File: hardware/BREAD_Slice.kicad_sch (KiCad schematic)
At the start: 15 parts, among them J1 Conn_01x10_Female, J2 I2C_01x04

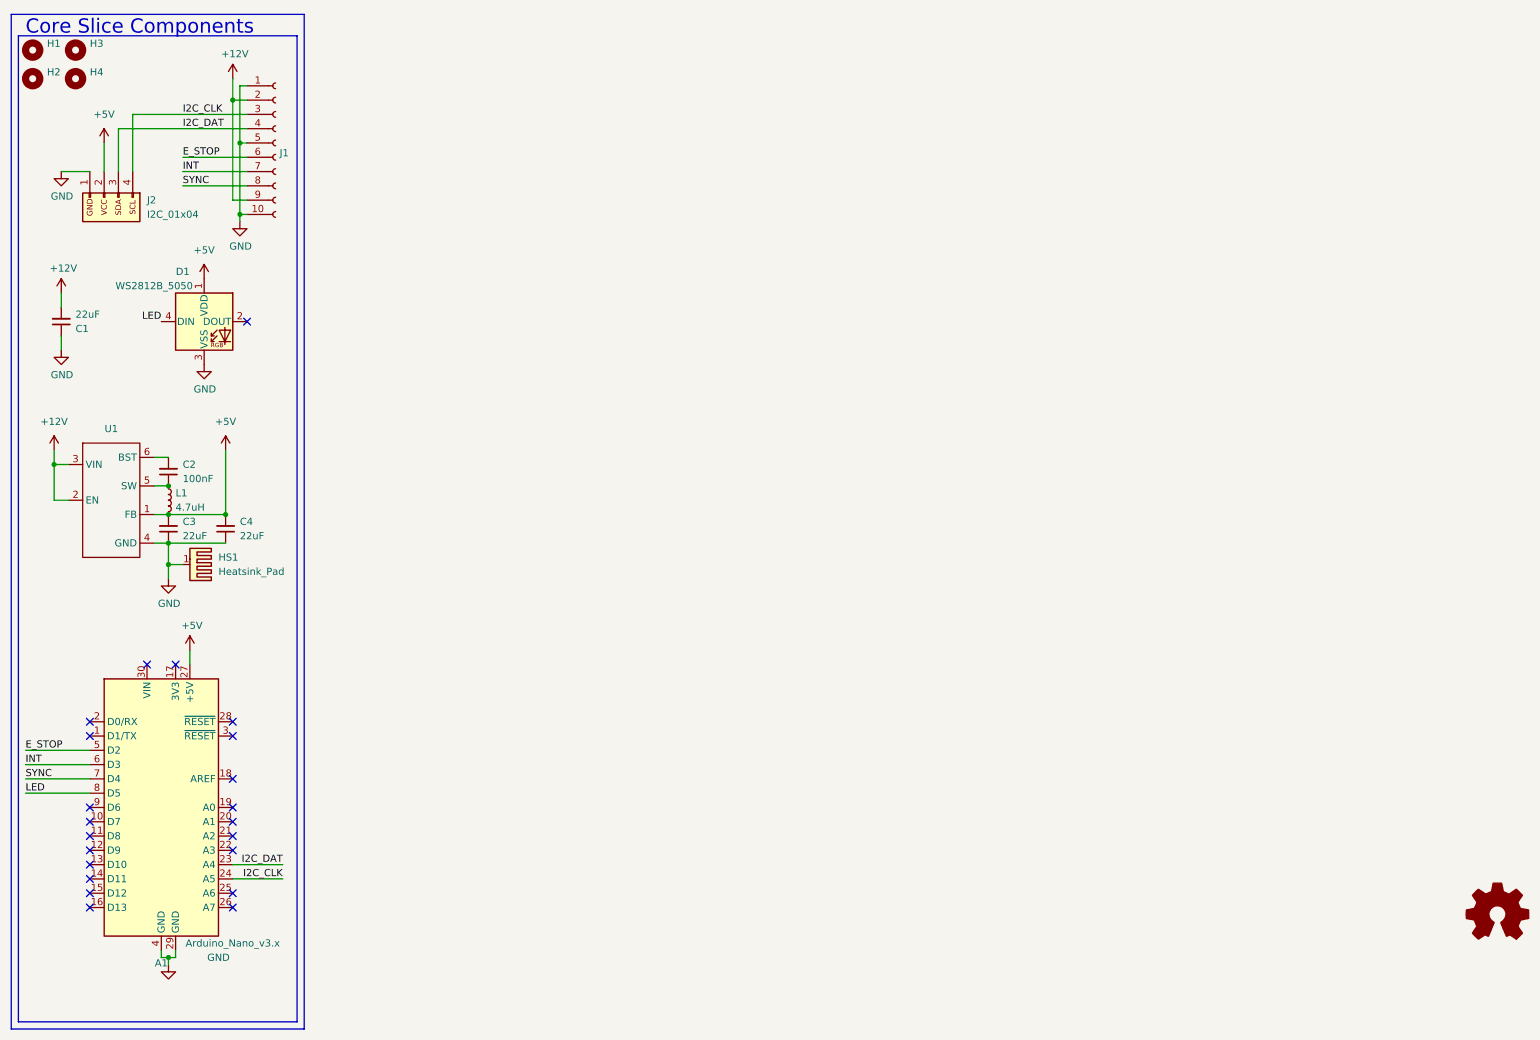
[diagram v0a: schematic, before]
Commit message: updated + checked schem and pcb with updated template
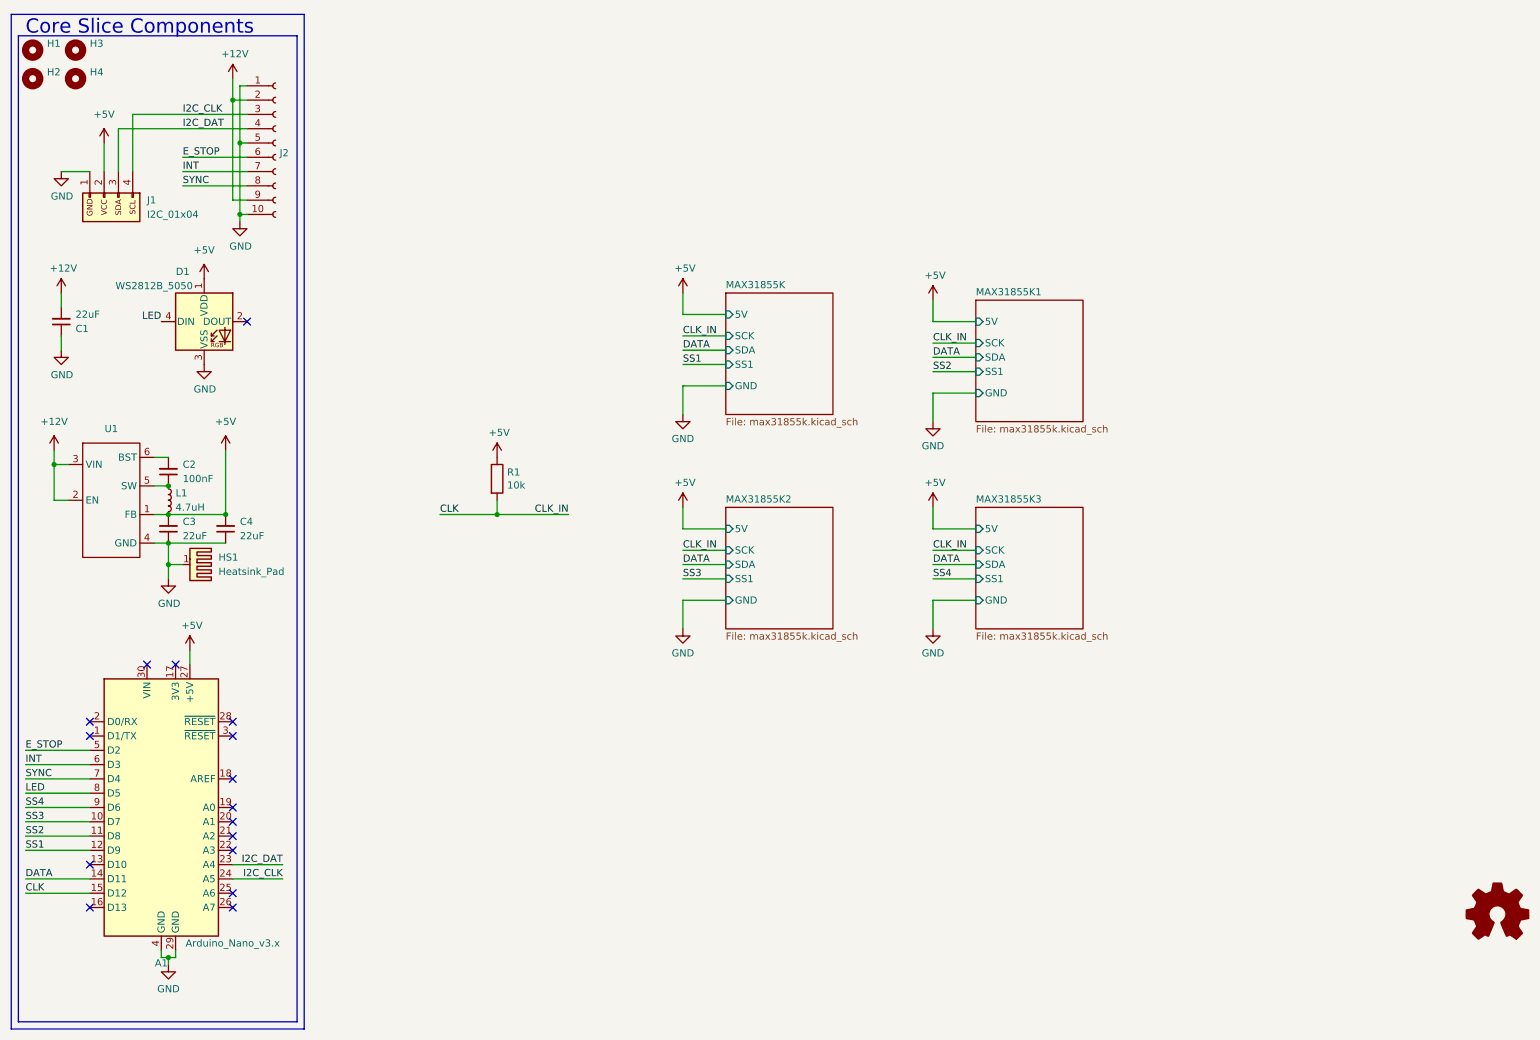
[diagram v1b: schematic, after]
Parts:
- added R1: 10k, Resistor_SMD:R_1206_3216Metric_Pad1.30x1.75mm_HandSolder, symbol Device:R
- HS1: footprint SparkFun-Fuse:Thermal Pad -> KML-Custom:Thermal Pad
- renumbered J2 to J1, J1 to J2
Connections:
- net +5V: now also R1.1
- net SS3: now reaches A1.10 (D7)
- net SS2: now reaches A1.11 (D8)
- net SS1: now reaches A1.12 (D9)
- net DATA: now reaches A1.14 (D11)
- net CLK: now reaches A1.15 (D12)
- net CLK: now also R1.2
- net SS4: now reaches A1.9 (D6)
- no-connect marks 22 -> 16
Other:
- added sheet MAX31855K (max31855k.kicad_sch)
- added sheet MAX31855K1 (max31855k.kicad_sch)
- added sheet MAX31855K2 (max31855k.kicad_sch)
- added sheet MAX31855K3 (max31855k.kicad_sch)

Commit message: removed unneeded top level 10k clk pull up (one on each max already
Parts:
- removed R1: 10k, Resistor_SMD:R_1206_3216Metric_Pad1.30x1.75mm_HandSolder, symbol Device:R
